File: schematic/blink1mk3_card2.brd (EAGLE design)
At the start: 99 x 50.9 mm, 39 parts, among them J1 NONPOP, U1 EFM32HG309F64G, X1 USBPCB2SIDE, X2 USBPCB2

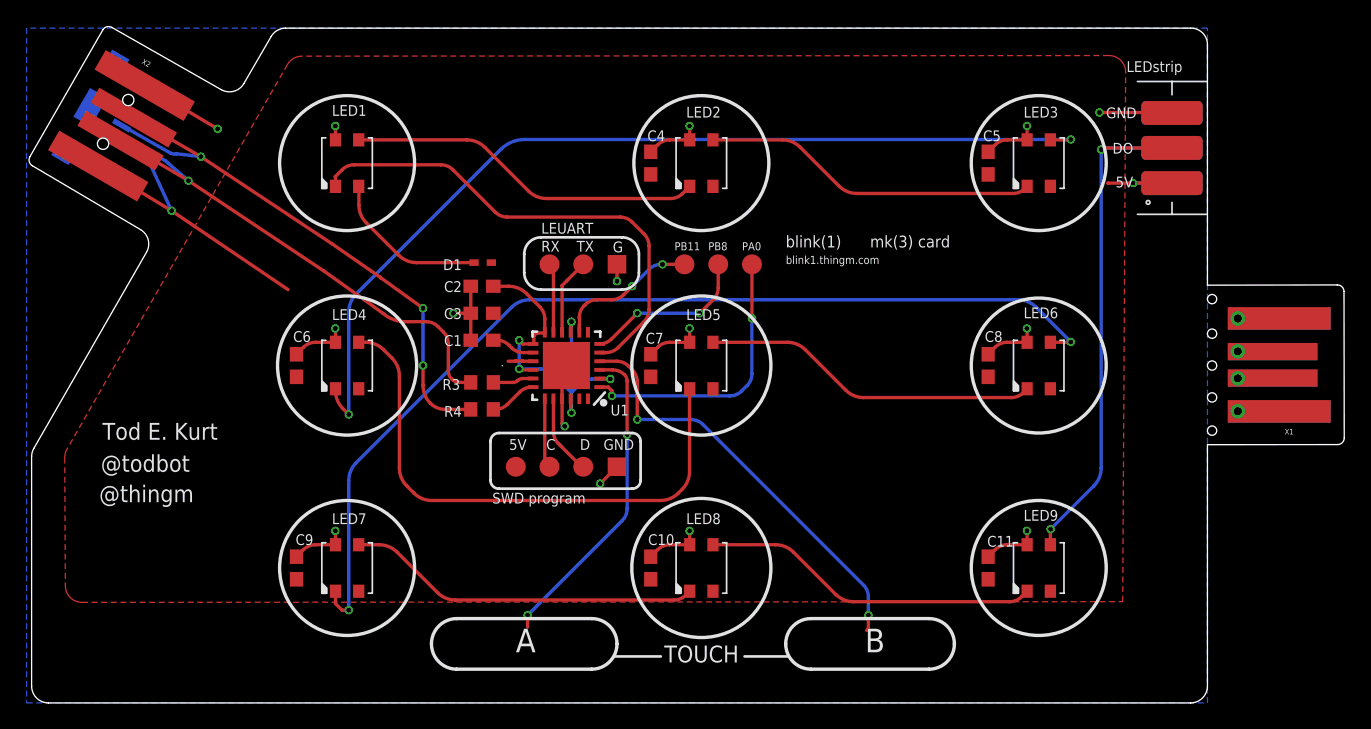
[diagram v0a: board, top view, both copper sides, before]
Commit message: small blink1mk3_card2 pcb fixes
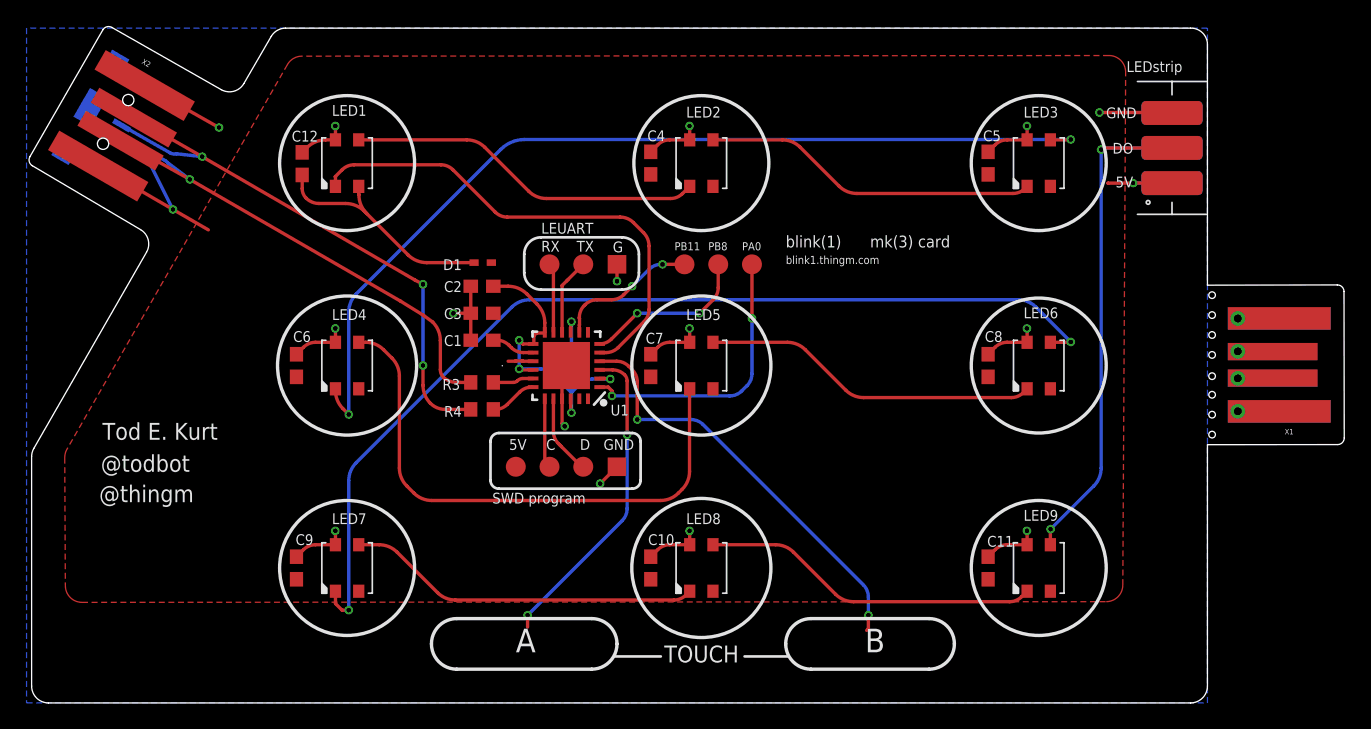
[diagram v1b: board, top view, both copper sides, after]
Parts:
- added C12: 0.1uF, adafruit:C0603
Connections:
- net GND: now also C12.2
- net VLEDA: now also C12.1
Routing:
- net +5V: track 33.9 -> 26.4 mm
- net VLEDA: track 12.1 -> 18.3 mm
- net GND: track 60.4 -> 63.2 mm
- net USB_D+: track 43.0 -> 44.0 mm
